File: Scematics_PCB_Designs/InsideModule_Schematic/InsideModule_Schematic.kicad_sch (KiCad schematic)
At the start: 7 parts, among them SW1 Push_Displ, SW2 Push_Set, U1 DHT22, U2 ESP32-DevKitC, U3 NRF24L01_Breakout

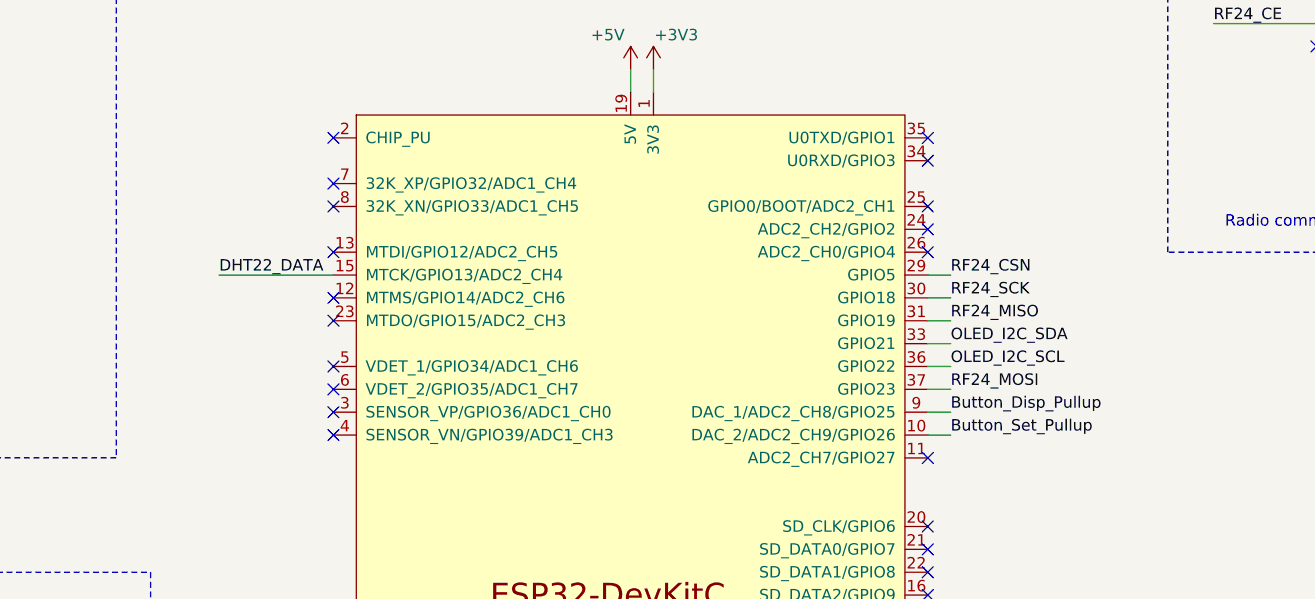
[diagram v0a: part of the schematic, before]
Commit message: Finalized code
-Wifi connectivity (capability for storing several networks
- HTTPS request sender for logging the data
- Calibrated snow meter
- Added NTC time server receiver on inside module
- Moved buttons to different pins (previous were used by WiFi)
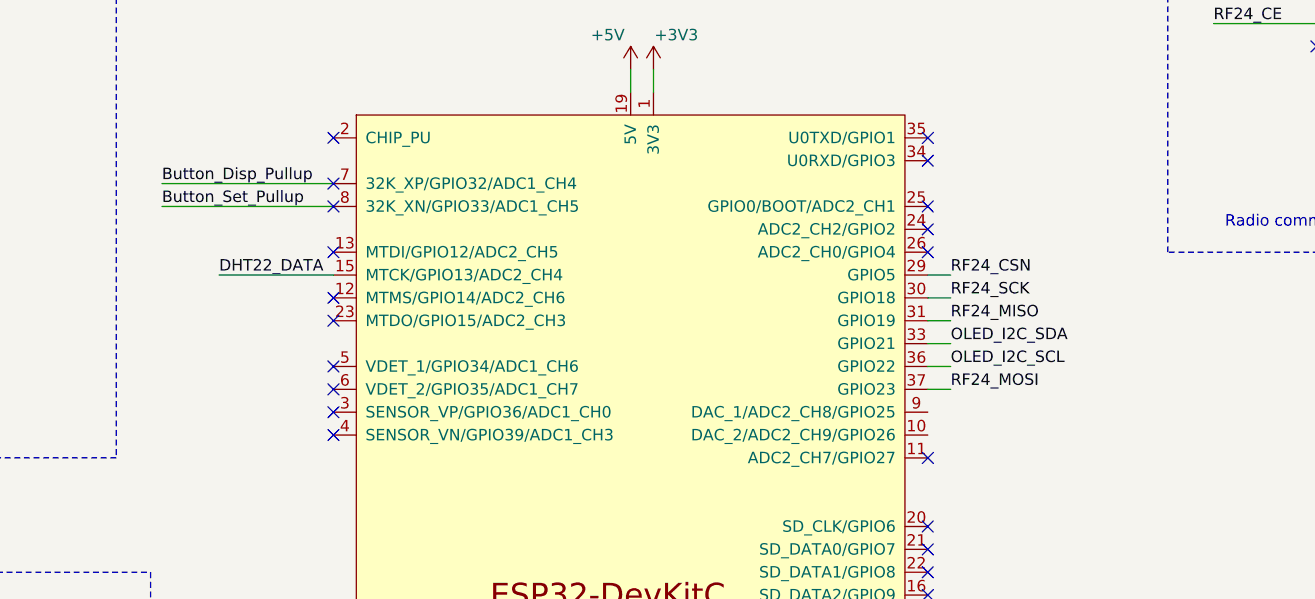
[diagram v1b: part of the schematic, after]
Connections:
- net Button_Disp_Pullup: now also U2.7 (32K_XP/GPIO32/ADC1_CH4); no longer U2.9 (DAC_1/ADC2_CH8/GPIO25)
- net Button_Set_Pullup: now also U2.8 (32K_XN/GPIO33/ADC1_CH5); no longer U2.10 (DAC_2/ADC2_CH9/GPIO26)
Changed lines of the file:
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@@
+    (stroke (width 0) (type default))
+  )
+  (wire (pts (xy 93.98 81.28) (xy 113.03 81.28))
     (stroke (width 0) (type default))
   )
@@
   )
   (wire (pts (xy 148.59 66.04) (xy 148.59 68.58))
-    (stroke (width 0) (type default))
-  )
-  (wire (pts (xy 181.61 104.14) (xy 179.07 104.14))
     (stroke (width 0) (type default))
   )
@@
     (stroke (width 0) (type default))
   )
-  (wire (pts (xy 179.07 106.68) (xy 181.61 106.68))
+  (wire (pts (xy 93.98 78.74) (xy 113.03 78.74))
     (stroke (width 0) (type default))
   )
@@
     (effects (font (size 1.27 1.27)) (justify left bottom))
   )
+  (label "Button_Disp_Pullup" (at 93.98 78.74 0) (fields_autoplaced)
+    (effects (font (size 1.27 1.27)) (justify left bottom))
+  )
   (label "RF24_MISO" (at 181.61 93.98 0) (fields_autoplaced)
     (effects (font (size 1.27 1.27)) (justify left bottom))
@@
     (effects (font (size 1.27 1.27)) (justify left bottom))
   )
-  (label "Button_Set_Pullup" (at 181.61 106.68 0) (fields_autoplaced)
+  (label "OLED_I2C_SCL" (at 72.39 43.18 0) (fields_autoplaced)
     (effects (font (size 1.27 1.27)) (justify left bottom))
   )
-  (label "OLED_I2C_SCL" (at 72.39 43.18 0) (fields_autoplaced)
+  (label "Button_Set_Pullup" (at 93.98 81.28 0) (fields_autoplaced)
     (effects (font (size 1.27 1.27)) (justify left bottom))
   )
@@
     (effects (font (size 1.27 1.27)) (justify left bottom))
   )
-  (label "Button_Disp_Pullup" (at 181.61 104.14 0) (fields_autoplaced)
-    (effects (font (size 1.27 1.27)) (justify left bottom))
-  )
